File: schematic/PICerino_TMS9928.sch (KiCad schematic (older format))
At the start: 80 parts, among them CON1 PICERINO-EDGE, IC1 ADG453BNZ, J1 Conn_01x02, J10 Conn_01x08, J11 Conn_01x08, J12 Conn_01x03, J2 Y_Conn_01x02, J3 BY_Conn_01x02, J4 RY_Conn_01x02, J5 Conn_01x02, J6 Y_Conn_DC_FIX_01x02, J7 Conn_01x02, J8 Conn_01x02, J9 Conn_01x02, U1 LM1881, Y1 Crystal

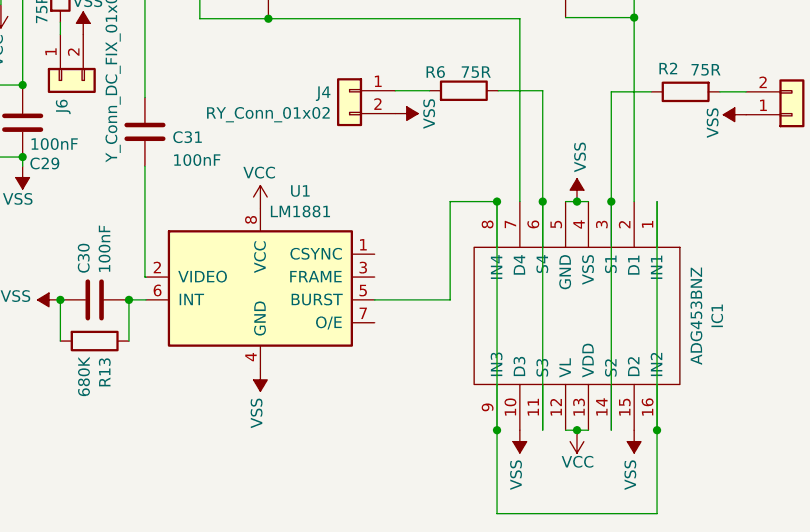
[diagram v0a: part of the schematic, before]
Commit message: added two connectors to break out lm1881 outputs. essentially this is so outputs can be setup to particular use case. this is not a great video circuit, the routing is sloppy in this version.
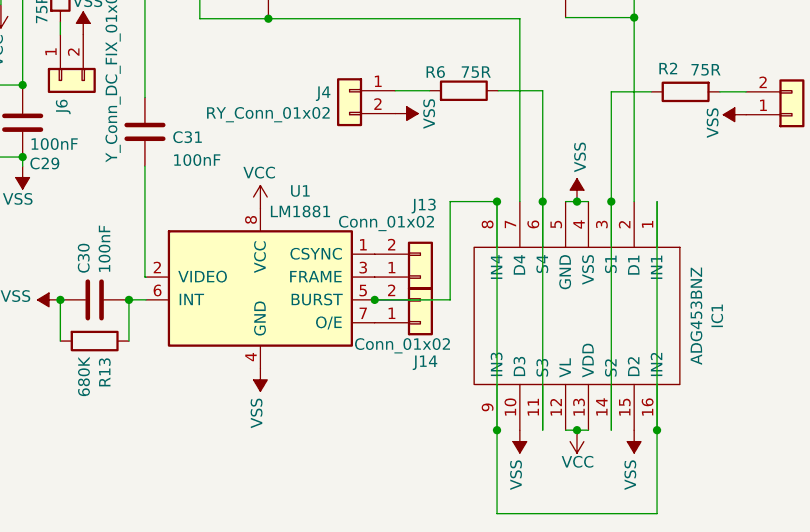
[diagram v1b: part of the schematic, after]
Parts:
- added J13, J14: Conn_01x02, Connector_PinHeader_2.54mm:PinHeader_1x02_P2.54mm_Vertical, symbol Connector_Generic:Conn_01x02
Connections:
- net at U1.1 (CSYNC): now also J13.2 (Pin_2)
- net at U1.3 (FRAME): now also J13.1 (Pin_1)
- net at IC1.1 (IN1), IC1.16 (IN2), IC1.8 (IN4)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: now also J14.2 (Pin_2)
- net at U1.7 (O/E): now also J14.1 (Pin_1)
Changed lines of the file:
@@
 Wire Bus Line
 	3500 3550 3500 4250
+$Comp
+L Connector_Generic:Conn_01x02 J13
+U 1 1 627060A9
+P 6835 9360
+F 0 "J13" H 6800 9045 50  0000 L CNN
+F 1 "Conn_01x02" H 6475 9120 50  0000 L CNN
+F 2 "Connector_PinHeader_2.54mm:PinHeader_1x02_P2.54mm_Vertical" H 6835 9360 50  0001 C CNN
+F 3 "~" H 6835 9360 50  0001 C CNN
+	1    6835 9360
+	1    0    0    1
+$EndComp
+$Comp
+L Connector_Generic:Conn_01x02 J14
+U 1 1 62708C59
+P 6835 9560
+F 0 "J14" H 6805 9730 50  0000 L CNN
+F 1 "Conn_01x02" H 6545 9655 50  0000 L CNN
+F 2 "Connector_PinHeader_2.54mm:PinHeader_1x02_P2.54mm_Vertical" H 6835 9560 50  0001 C CNN
+F 3 "~" H 6835 9560 50  0001 C CNN
+	1    6835 9560
+	1    0    0    1
+$EndComp
+Connection ~ 6635 9460
 $EndSCHEMATC

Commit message: major change to video circuit, first working version that does not suffer from over blue issue. This has only been tested to work with the retrotink x2. Since most YrYbY do not accept 240p and it needs to be upscaled. Values for the 2.7v DC bias zener diode circuit will be finalized soon when they arrive (makeshift circuit in use at the moment.. 5-3.3 oh yeah ;))
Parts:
- removed C10, C4, C7: 22uF, Capacitor_THT:CP_Radial_D5.0mm_P2.00mm, symbol Device:CP
- removed C11, C27, C5, C8: 100uF, Capacitor_THT:CP_Radial_D7.5mm_P2.50mm, symbol Device:CP
- removed C28, C3: 10uF, Capacitor_THT:CP_Radial_D5.0mm_P2.00mm, symbol Device:CP
- removed C30, C31: 100nF, Capacitor_THT:C_Disc_D4.7mm_W2.5mm_P5.00mm, symbol Device:C
- removed C6, C9: 4.7uF, Capacitor_THT:CP_Radial_D5.0mm_P2.00mm, symbol Device:CP
- removed D1, D2, D3: 1N914, Diode_THT:D_DO-35_SOD27_P7.62mm_Horizontal, symbol Diode:1N914
- removed J13, J14, J8, J9: Conn_01x02, Connector_PinHeader_2.54mm:PinHeader_1x02_P2.54mm_Vertical, symbol Connector_Generic:Conn_01x02
- removed J2: Y_Conn_01x02, Connector_PinHeader_2.54mm:PinHeader_1x02_P2.54mm_Vertical, symbol Connector_Generic:Conn_01x02
- removed J3: BY_Conn_01x02, Connector_PinHeader_2.54mm:PinHeader_1x02_P2.54mm_Vertical, symbol Connector_Generic:Conn_01x02
- removed J4: RY_Conn_01x02, Connector_PinHeader_2.54mm:PinHeader_1x02_P2.54mm_Vertical, symbol Connector_Generic:Conn_01x02
- removed R4, R5: 1M, Resistor_THT:R_Axial_DIN0207_L6.3mm_D2.5mm_P7.62mm_Horizontal, symbol Device:R
- removed R6: 75R, Resistor_THT:R_Axial_DIN0207_L6.3mm_D2.5mm_P2.54mm_Vertical, symbol Device:R
- removed RV1: 100R, Potentiometer_THT:Potentiometer_Piher_PT-6-V_Vertical_Hole, symbol Device:R_POT_TRIM
- removed RV2, RV3, RV4: 10K, Potentiometer_THT:Potentiometer_Piher_PT-6-V_Vertical_Hole, symbol Device:R_POT_TRIM
- removed V2, V3: NJM2267, Package_SO:SSOP-8_3.9x5.05mm_P1.27mm, symbol VINTAGE_PC_VIDEO:NJM2267
- added C12, C15: 100nF, Capacitor_THT:C_Disc_D4.7mm_W2.5mm_P5.00mm, symbol Device:C
- added C14: 10uF, Capacitor_THT:CP_Radial_D5.0mm_P2.50mm, symbol Device:CP_Small
- added C23, C26, C27: 33uF, Capacitor_THT:CP_Radial_D5.0mm_P2.50mm, symbol Device:CP_Small
- added C24, C25, C28: 470uF, Capacitor_THT:CP_Radial_D8.0mm_P5.00mm, symbol Device:CP_Small
- added D1: D_Zener_2-7, Diode_THT:D_DO-34_SOD68_P7.62mm_Horizontal, symbol Device:D_Zener
- added IC2: AD813ANZ, Package_DIP:DIP-14_W7.62mm_LongPads, symbol AD813ANZ:AD813ANZ
- added J1, J2, J4: Conn_01x03, Connector_PinHeader_2.54mm:PinHeader_1x03_P2.54mm_Vertical, symbol Connector_Generic:Conn_01x03
- added R14, R7, R8: 510R, Resistor_THT:R_Axial_DIN0207_L6.3mm_D2.5mm_P7.62mm_Horizontal, symbol Device:R
- added R15, R9: 75R, Resistor_THT:R_Axial_DIN0207_L6.3mm_D2.5mm_P7.62mm_Horizontal, symbol Device:R
- added RV1: R_POT, Potentiometer_THT:Potentiometer_Piher_PT-6-V_Vertical, symbol Device:R_POT
- added TP1, TP2: TestPoint, Connector_PinHeader_2.54mm:PinHeader_1x01_P2.54mm_Vertical, symbol Connector:TestPoint
- IC1: value ADG453BNZ -> ADG453/413; footprint Package_SO:SOIC-16_3.9x9.9mm_P1.27mm -> Package_DIP:DIP-16_W7.62mm_LongPads
- J5: value Conn_01x02 -> Conn_01x02_Yr
- J6: value Y_Conn_DC_FIX_01x02 -> Conn_01x02_Y
- J7: value Conn_01x02 -> Conn_01x02_Yb
- R1: value 75R -> 1K; footprint Resistor_THT:R_Axial_DIN0207_L6.3mm_D2.5mm_P2.54mm_Vertical -> Resistor_THT:R_Axial_DIN0207_L6.3mm_D2.5mm_P7.62mm_Horizontal
- R10: value 470R -> 510R
- R11: value 1M -> 510R
- R12: footprint Resistor_THT:R_Axial_DIN0207_L6.3mm_D2.5mm_P2.54mm_Vertical -> Resistor_THT:R_Axial_DIN0207_L6.3mm_D2.5mm_P7.62mm_Horizontal
- R13: value 680K -> 510R
- R2: value 75R -> 470R; footprint Resistor_THT:R_Axial_DIN0207_L6.3mm_D2.5mm_P2.54mm_Vertical -> Resistor_THT:R_Axial_DIN0207_L6.3mm_D2.5mm_P7.62mm_Horizontal
- R3: value 1M -> 680k
- renumbered C32 to C1, C1 to C10, C2 to C11, C21 to C13, C22 to C16, C23 to C17, C12 to C18, C13 to C19, C33 to C2, C24 to C20, C14 to C21, C25 to C22, C15 to C3, C16 to C4, C17 to C5, C18 to C6, C19 to C7, C20 to C8, C26 to C9, J12 to J10, J1 to J3, J10 to J8, J11 to J9, R7 to R4, R8 to R5, R9 to R6, V4 to V2, V5 to V3, V6 to V4, V7 to V5, V8 to V6, V9 to V7, V10 to V8, V11 to V9
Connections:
- net VCC: now also R1.2, R2.2, IC2.1 (~DISABLE1), IC2.2 (~DISABLE2), IC2.3 (~DISABLE3), IC2.4 (VS+); no longer R10.1
- net VSS: now also C29.2, J5.2 (Pin_2), J7.2 (Pin_2), C12.2, C14.2, C23.2, C26.2, C27.2, D1.2 (A), IC2.11 (VS-), J1.3 (Pin_3), J2.1 (Pin_1), J4.3 (Pin_3); no longer C29.1, IC1.10 (D3), IC1.15 (D2), R11.1, R13.2
- net Y: now also C15.1, J4.1 (Pin_1)
- net Yb: now also J2.3 (Pin_3)
- net Yr: now also J1.1 (Pin_1)
- net at R3.2: now also U1.6 (INT), C12.1
- net at R12.1: now also C25.1
- net at R11.2: now also IC2.9 (-IN3), R14.2
- net at R1.1: now also IC1.1 (IN1), IC1.16 (IN2), IC1.8 (IN4), IC1.9 (IN3), U1.5 (BURST), TP1.1
- net at J5.1 (Pin_1): now also C28.2; no longer J7.1 (Pin_1)
- net at U1.2 (VIDEO): now also C15.2
- net at R13.1: now also R10.1, IC2.13 (-IN2); no longer U1.6 (INT)
- net at IC1.11 (S3), IC1.6 (S4): now also IC2.10 (+IN3)
- net at IC1.14 (S2), IC1.3 (S1): now also IC2.5 (+IN1); no longer R2.1
- net at IC1.2 (D1): now also J2.2 (Pin_2)
- net at IC1.7 (D4): now also J1.2 (Pin_2)
- net at R12.2: now also R10.2, IC2.14 (OUT2); no longer J6.1 (Pin_1)
- new net: IC2.12 (+IN2), J4.2 (Pin_2)
- new net: IC2.6 (-IN1), R7.1, R8.1
- new net: IC2.7 (OUT1), R8.2, R9.2
- new net: IC2.8 (OUT3), R11.1, R15.2
- new net: C14.1, C29.1, IC1.10 (D3), IC1.15 (D2), R2.1, RV1.1, TP2.1
- new net: C25.2, J6.1 (Pin_1)
- new net: D1.1 (K), RV1.2, RV1.3
- new net: C26.1, R13.2
- new net: C23.1, R7.2
- new net: C24.1, R9.1
- new net: C24.2, J7.1 (Pin_1)
- new net: C27.1, R14.1
- new net: C28.1, R15.1
- no-connect marks 0 -> 3
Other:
- moved on the sheet: C1, C13, C16, C17, C2, C20, C22, C3, C4, C5, C6, C7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

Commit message: added a bleader resistor, still need to test the circuit before creating final board.
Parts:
- removed J5: Conn_01x02_Yr, Connector_PinHeader_2.54mm:PinHeader_1x02_P2.54mm_Vertical, symbol Connector_Generic:Conn_01x02
- removed J6: Conn_01x02_Y, Connector_PinHeader_2.54mm:PinHeader_1x02_P2.54mm_Vertical, symbol Connector_Generic:Conn_01x02
- removed J7: Conn_01x02_Yb, Connector_PinHeader_2.54mm:PinHeader_1x02_P2.54mm_Vertical, symbol Connector_Generic:Conn_01x02
- added J5: Conn_01x03_Yb, Connector_PinHeader_2.54mm:PinHeader_1x03_P2.54mm_Vertical, symbol Connector_Generic:Conn_01x03
- added J6: Conn_01x03_Y, Connector_PinHeader_2.54mm:PinHeader_1x03_P2.54mm_Vertical, symbol Connector_Generic:Conn_01x03
- added J7: Conn_01x03_Yr, Connector_PinHeader_2.54mm:PinHeader_1x03_P2.54mm_Vertical, symbol Connector_Generic:Conn_01x03
- added R16: 1M, Resistor_THT:R_Axial_DIN0207_L6.3mm_D2.5mm_P7.62mm_Horizontal, symbol Device:R
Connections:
- net VSS: now also J5.2 (Pin_2), J6.2 (Pin_2), J7.2 (Pin_2), R16.1
- net at C14.1, C29.1, IC1.10 (D3)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: now also R16.2
- net at C25.2: now also J6.3 (Pin_3)
- net at C25.1, R12.1: now also J6.1 (Pin_1)
- net at C28.2: now also J7.3 (Pin_3)
- net at C24.1, R9.1: now also J5.1 (Pin_1)
- net at C24.2: now also J5.3 (Pin_3)
- net at C28.1, R15.1: now also J7.1 (Pin_1)
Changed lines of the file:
@@
 	6250 6500 5725 6500
-$Comp
-L Connector_Generic:Conn_01x02 J6
-U 1 1 62D67FC6
-P 10475 7425
-F 0 "J6" H 10555 7417 50  0000 L CNN
-F 1 "Conn_01x02_Y" H 10555 7326 50  0000 L CNN
-F 2 "Connector_PinHeader_2.54mm:PinHeader_1x02_P2.54mm_Vertical" H 10475 7425 50  0001 C CNN
-F 3 "~" H 10475 7425 50  0001 C CNN
-	1    10475 7425
-	1    0    0    -1
-$EndComp
 $Comp
 L Device:R R12
@@
 L power:VSS #PWR038
 U 1 1 62E712D4
-P 10250 7525
-F 0 "#PWR038" H 10250 7375 50  0001 C CNN
-F 1 "VSS" V 10225 7700 50  0000 C CNN
-F 2 "" H 10250 7525 50  0001 C CNN
-F 3 "" H 10250 7525 50  0001 C CNN
-	1    10250 7525
+P 10525 7425
+F 0 "#PWR038" H 10525 7275 50  0001 C CNN
+F 1 "VSS" V 10500 7600 50  0000 C CNN
+F 2 "" H 10525 7425 50  0001 C CNN
+F 3 "" H 10525 7425 50  0001 C CNN
+	1    10525 7425
 	0    -1   -1   0
 $EndComp
@@
 Wire Wire Line
 	4900 6950 4850 6950
-Wire Wire Line
-	10275 7525 10250 7525
 $Comp
 L Device:CP_Small C25
@@
 $EndComp
 Wire Wire Line
-	9875 7425 9950 7425
-Wire Wire Line
-	10150 7425 10275 7425
+	9875 7425 9900 7425
 $Comp
 L Device:R R10
@@
 Wire Wire Line
 	7450 7000 7450 7150
-Wire Wire Line
-	7550 7000 7550 7150
 $Comp
 L power:VSS #PWR028
@@
 	0    1    1    0
 $EndComp
-Wire Wire Line
-	7650 7075 7650 7000
 Wire Wire Line
 	9500 7425 9500 7825
@@
 L power:VSS #PWR06
 U 1 1 6338804C
-P 4075 8175
-F 0 "#PWR06" H 4075 8025 50  0001 C CNN
-F 1 "VSS" V 4075 8350 50  0000 C CNN
-F 2 "" H 4075 8175 50  0001 C CNN
-F 3 "" H 4075 8175 50  0001 C CNN
-	1    4075 8175
+P 3975 8200
+F 0 "#PWR06" H 3975 8050 50  0001 C CNN
+F 1 "VSS" V 3975 8375 50  0000 C CNN
+F 2 "" H 3975 8200 50  0001 C CNN
+F 3 "" H 3975 8200 50  0001 C CNN
+	1    3975 8200
 	0    -1   -1   0
 $EndComp
@@
 	7600 8425 7575 8425
 $Comp
-L Connector_Generic:Conn_01x02 J5
-U 1 1 63500FBA
-P 11300 8775
-F 0 "J5" H 11380 8767 50  0000 L CNN
-F 1 "Conn_01x02_Yr" H 11380 8676 50  0000 L CNN
-F 2 "Connector_PinHeader_2.54mm:PinHeader_1x02_P2.54mm_Vertical" H 11300 8775 50  0001 C CNN
-F 3 "~" H 11300 8775 50  0001 C CNN
-	1    11300 8775
-	1    0    0    -1
-$EndComp
-$Comp
 L Device:R R9
 U 1 1 63500FC0
@@
 L power:VSS #PWR032
 U 1 1 63500FC6
-P 8775 8875
-F 0 "#PWR032" H 8775 8725 50  0001 C CNN
-F 1 "VSS" V 8750 9050 50  0000 C CNN
-F 2 "" H 8775 8875 50  0001 C CNN
-F 3 "" H 8775 8875 50  0001 C CNN
-	1    8775 8875
-	0    -1   -1   0
-$EndComp
-Wire Wire Line
-	8800 8875 8775 8875
+P 9000 8775
+F 0 "#PWR032" H 9000 8625 50  0001 C CNN
+F 1 "VSS" V 8975 8950 50  0000 C CNN
+F 2 "" H 9000 8775 50  0001 C CNN
+F 3 "" H 9000 8775 50  0001 C CNN
+	1    9000 8775
+	0    -1   -1   0
+$EndComp
 $Comp
 L Device:CP_Small C24
@@
 $EndComp
 Wire Wire Line
-	8400 8775 8475 8775
-Wire Wire Line
-	8675 8775 8800 8775
+	8400 8775 8450 8775
 Wire Wire Line
 	7950 8425 7950 8775
@@
 Connection ~ 7975 8125
 $Comp
-L Connector_Generic:Conn_01x02 J7
-U 1 1 637D8F5D
-P 9000 8775
-F 0 "J7" H 9080 8767 50  0000 L CNN
-F 1 "Conn_01x02_Yb" H 9080 8676 50  0000 L CNN
-F 2 "Connector_PinHeader_2.54mm:PinHeader_1x02_P2.54mm_Vertical" H 9000 8775 50  0001 C CNN
-F 3 "~" H 9000 8775 50  0001 C CNN
-	1    9000 8775
-	1    0    0    -1
-$EndComp
-$Comp
 L Device:R R15
 U 1 1 637D8F63
@@
 L power:VSS #PWR043
 U 1 1 637D8F69
-P 11075 8875
-F 0 "#PWR043" H 11075 8725 50  0001 C CNN
-F 1 "VSS" V 11050 9050 50  0000 C CNN
-F 2 "" H 11075 8875 50  0001 C CNN
-F 3 "" H 11075 8875 50  0001 C CNN
-	1    11075 8875
-	0    -1   -1   0
-$EndComp
-Wire Wire Line
-	11100 8875 11075 8875
+P 11250 8775
+F 0 "#PWR043" H 11250 8625 50  0001 C CNN
+F 1 "VSS" V 11225 8950 50  0000 C CNN
+F 2 "" H 11250 8775 50  0001 C CNN
+F 3 "" H 11250 8775 50  0001 C CNN
+	1    11250 8775
+	0    -1   -1   0
+$EndComp
 $Comp
 L Device:CP_Small C28
@@
 $EndComp
 Wire Wire Line
-	10700 8775 10775 8775
-Wire Wire Line
-	10975 8775 11100 8775
+	10700 8775 10750 8775
 Wire Wire Line
 	9525 8775 9525 8425
@@
 Wire Wire Line
 	9525 8425 9550 8425
-Wire Wire Line
-	11975 8975 11975 8225
-Wire Wire Line
-	9475 8225 11975 8225
-Wire Wire Line
-	11125 8025 11125 7150
-Wire Wire Line
-	9475 8025 11125 8025
-Wire Wire Line
-	7550 7150 11125 7150
 $Comp
 L Connector:TestPoint TP2
@@
 	-1   0    0    1
 $EndComp
-Connection ~ 4075 8175
-Wire Wire Line
-	4075 8175 4075 8100
 Wire Wire Line
 	5200 8000 6200 8000
 Wire Wire Line
-	4175 8325 4175 8250
-Wire Wire Line
-	4075 8175 4075 8325
-Wire Wire Line
 	4625 7400 6350 7400
 Wire Wire Line
@@
 Wire Wire Line
 	4725 7500 6450 7500
-Wire Wire Line
-	6550 8975 11975 8975
 Wire Wire Line
 	6200 8300 6550 8300
@@
 Connection ~ 5625 8700
 Wire Wire Line
-	5625 8700 6450 8700
+	5625 8700 6200 8700
 $Comp
 L power:VSS #PWR0101
@@
 	4825 8400 5200 8400
 Wire Wire Line
+	4975 7900 5200 7900
+Wire Wire Line
+	4975 7900 4975 8250
+$Comp
+L Connector_Generic:Conn_01x03 J6
+U 1 1 62A9CE58
+P 10725 7425
+F 0 "J6" H 10875 7425 50  0000 R CNN
+F 1 "Conn_01x03_Y" H 11325 7325 50  0000 R CNN
+F 2 "Connector_PinHeader_2.54mm:PinHeader_1x03_P2.54mm_Vertical" H 10725 7425 50  0001 C CNN
+F 3 "~" H 10725 7425 50  0001 C CNN
+	1    10725 7425
+	1    0    0    -1
+$EndComp
+Wire Wire Line
+	10275 7325 10275 7200
+Wire Wire Line
+	10275 7200 9900 7200
+Wire Wire Line
+	9900 7200 9900 7425
+Connection ~ 9900 7425
+Wire Wire Line
+	9900 7425 9950 7425
+$Comp
+L Connector_Generic:Conn_01x03 J7
+U 1 1 62AD1BC1
+P 11450 8775
+F 0 "J7" H 11600 8825 50  0000 R CNN
+F 1 "Conn_01x03_Yr" H 12075 8675 50  0000 R CNN
+F 2 "Connector_PinHeader_2.54mm:PinHeader_1x03_P2.54mm_Vertical" H 11450 8775 50  0001 C CNN
+F 3 "~" H 11450 8775 50  0001 C CNN
+	1    11450 8775
+	1    0    0    -1
+$EndComp
+Wire Wire Line
+	11050 8675 11050 8525
+Wire Wire Line
+	11050 8525 10750 8525
+Wire Wire Line
+	10750 8525 10750 8775
+Connection ~ 10750 8775
+Wire Wire Line
+	10750 8775 10775 8775
+$Comp
+L Connector_Generic:Conn_01x03 J5
+U 1 1 62B07ED5
+P 9200 8775
+F 0 "J5" H 9350 8825 50  0000 R CNN
+F 1 "Conn_01x03_Yb" H 9850 8675 50  0000 R CNN
+F 2 "Connector_PinHeader_2.54mm:PinHeader_1x03_P2.54mm_Vertical" H 9200 8775 50  0001 C CNN
+F 3 "~" H 9200 8775 50  0001 C CNN
+	1    9200 8775
+	1    0    0    -1
+$EndComp
+Wire Wire Line
+	8800 8675 8800 8550
+Wire Wire Line
+	8800 8550 8450 8550
+Wire Wire Line
+	8450 8550 8450 8775
+Connection ~ 8450 8775
+Wire Wire Line
+	8450 8775 8475 8775
+$Comp
+L Device:R R16
+U 1 1 62AB4DAE
+P 6200 8850
+F 0 "R16" V 6300 8775 50  0000 L CNN
+F 1 "1M" V 6100 8800 50  0000 L CNN
+F 2 "Resistor_THT:R_Axial_DIN0207_L6.3mm_D2.5mm_P7.62mm_Horizontal" V 6130 8850 50  0001 C CNN
+F 3 "~" H 6200 8850 50  0001 C CNN
+	1    6200 8850
+	-1   0    0    1
+$EndComp
+Connection ~ 6200 8700
+Wire Wire Line
+	6200 8700 6450 8700
+$Comp
+L power:VSS #PWR0102
+U 1 1 62AB52D0
+P 6200 9000
+F 0 "#PWR0102" H 6200 8850 50  0001 C CNN
+F 1 "VSS" V 6275 9100 50  0000 C CNN
+F 2 "" H 6200 9000 50  0001 C CNN
+F 3 "" H 6200 9000 50  0001 C CNN
+	1    6200 9000
+	-1   0    0    1
+$EndComp
+Wire Wire Line
+	4825 8150 4175 8150
+Wire Wire Line
 	4175 8150 4175 8100
 Wire Wire Line
-	4175 8150 4825 8150
-Wire Wire Line
-	4175 8250 4975 8250
-Wire Wire Line
-	4975 7900 5200 7900
-Wire Wire Line
-	4975 7900 4975 8250
+	4975 8250 4175 8250
+Wire Wire Line
+	4175 8250 4175 8325
+Wire Wire Line
+	4075 8325 4075 8200
+Wire Wire Line
+	3975 8200 4075 8200
+Connection ~ 4075 8200
+Wire Wire Line
+	4075 8200 4075 8100
+Wire Wire Line
+	7550 7150 7550 7000
+Wire Wire Line
+	7650 7075 7650 7000
+Wire Wire Line
+	9000 8675 8800 8675
+Wire Wire Line
+	8675 8775 8675 8875
+Wire Wire Line
+	8675 8875 9000 8875
+Wire Wire Line
+	12125 8975 12125 8225
+Wire Wire Line
+	9475 8225 12125 8225
+Wire Wire Line
+	6550 8975 12125 8975
+Wire Wire Line
+	11050 8675 11250 8675
+Wire Wire Line
+	11250 8875 10975 8875
+Wire Wire Line
+	10975 8875 10975 8775
+Wire Wire Line
+	10525 7525 10150 7525
+Wire Wire Line
+	10150 7525 10150 7425
+Wire Wire Line
+	10275 7325 10525 7325
+Wire Wire Line
+	11375 8025 11375 7150
+Wire Wire Line
+	9475 8025 11375 8025
+Wire Wire Line
+	7550 7150 11375 7150
 Wire Bus Line
 	13700 2350 13700 3900
